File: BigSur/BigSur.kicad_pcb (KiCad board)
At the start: 2 copper layers, 123.5 x 131.5 mm, 148 parts, among them J1 XT30PW-M, J10 XT30PW-M, J12 XT30PW-M, J14 XT30PW-M, J15 XT30PW-M, J16 XT30PW-M, J2 XT30PW-M, J3 XT30PW-M, J4 XT30PW-M, J5 XT30PW-M, J6 XT30PW-M, J7 XT30PW-M, J8 XT30PW-M, J9 XT30PW-M, K1 G5LE-1A-VDDC12, K2 G5LE-1A-VDDC12, K3 G5LE-1A-VDDC12, K4 G5LE-1A-VDDC12, Q1 TSM900N10, Q2 TSM900N10, Q3 MMBT3904-7-F, Q4 MMBT3904-7-F, Q5 MMBT3904-7-F, Q6 MMBT3904-7-F, U1 DRV103H, U10 MCP6L02T-E_MS, U11 74LVC1G08W5-7, U12 ACS70331EESATR-2P5U3, U2 DRV103H, U3 DRV8806, U4 SMD46, U5 ACS70331EESATR-2P5U3, U6 ACS70331EESATR-2P5U3, U7 ACS70331EESATR-2P5U3, U8 ACS70331EESATR-2P5U3, U9 ACS70331EESATR-2P5U3

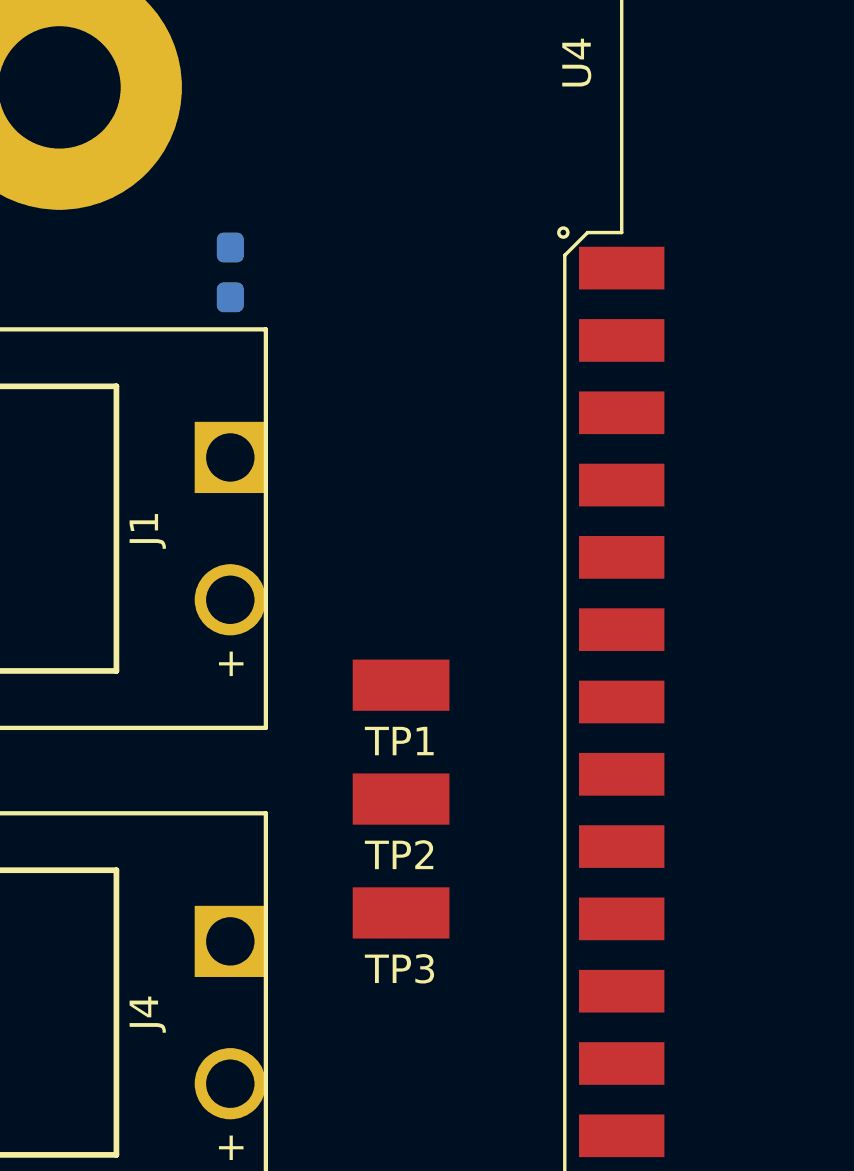
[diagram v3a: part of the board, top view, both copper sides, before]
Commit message: Added power LEDs.
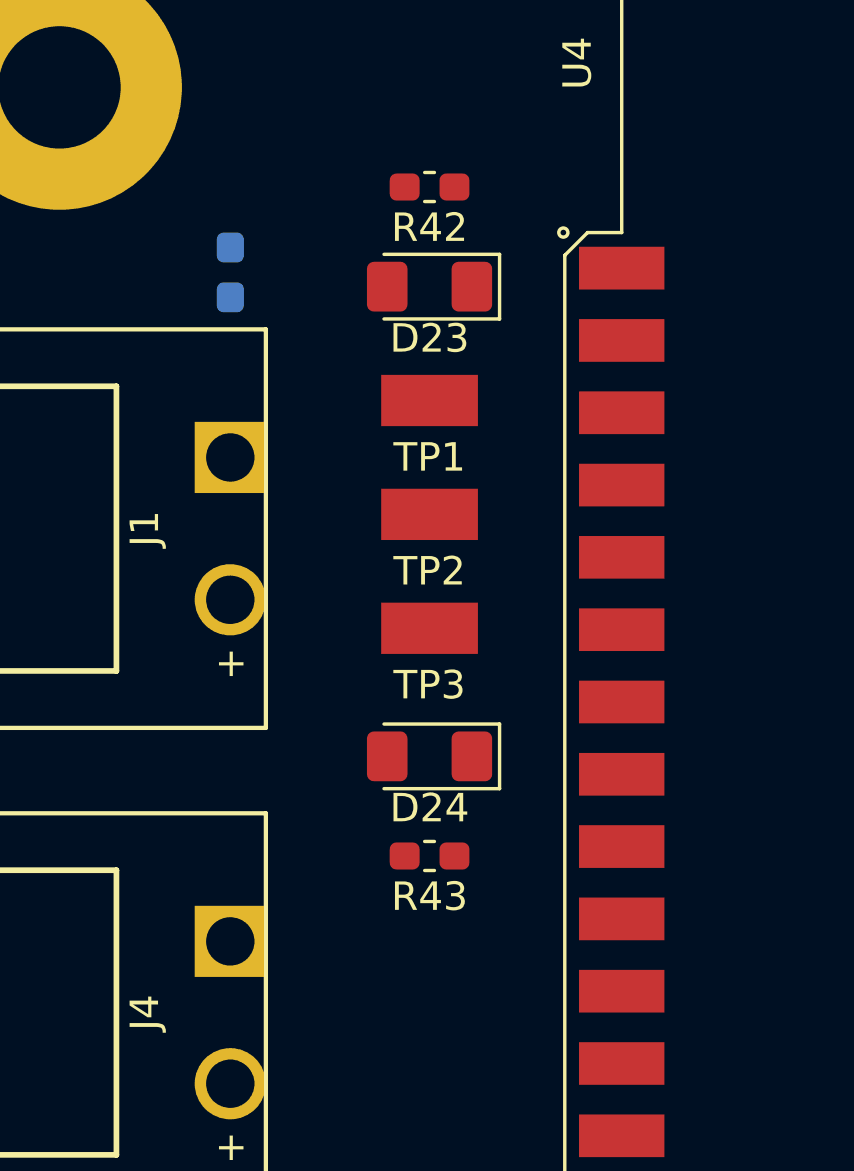
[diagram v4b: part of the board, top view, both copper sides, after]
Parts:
- added D23: QTLP651C4TR, LED_SMD:LED_1206_3216Metric_Pad1.42x1.75mm_HandSolder, F.Cu at (46.0, 34.5)
- added D24: QTLP651C4TR, LED_SMD:LED_1206_3216Metric_Pad1.42x1.75mm_HandSolder, F.Cu at (46.0, 51.0)
- added R42: 2K, Resistor_SMD:R_0603_1608Metric_Pad1.05x0.95mm_HandSolder, F.Cu at (46.0, 31.0)
- added R43: 1K, Resistor_SMD:R_0603_1608Metric_Pad1.05x0.95mm_HandSolder, F.Cu at (46.0, 54.5)
- moved TP1 10.0 mm to (46.0, 38.5)
- moved TP2 10.0 mm to (46.0, 42.5)
- moved TP3 10.0 mm to (46.0, 46.5)
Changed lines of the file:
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@@
     (tracks 0)
     (zones 0)
-    (modules 148)
-    (nets 116)
+    (modules 152)
+    (nets 118)
   )
   (page A4)
@@
   (net 114 "Net-(U10-Pad7)")
   (net 115 "Net-(U12-Pad7)")
+  (net 116 "Net-(D23-Pad1)")
+  (net 117 "Net-(D24-Pad1)")
   (net_class Default "This is the default net class."
     (clearance 0.2)
@@
     (add_net "Net-(D21-Pad2)")
     (add_net "Net-(D22-Pad2)")
+    (add_net "Net-(D23-Pad1)")
+    (add_net "Net-(D24-Pad1)")
     (add_net "Net-(D4-Pad2)")
     (add_net "Net-(D6-Pad2)")
@@
   )
   (module BigSur:Keystone_TP_SMD_5015 (layer F.Cu)
-    (at 45 48.5)
+    (at 46 38.5)
     (fp_text reference TP1 (at 0 2) (layer F.SilkS)
       (effects (font (size 1 1) (thickness 0.15)))
@@
   )
   (module BigSur:Keystone_TP_SMD_5015 (layer F.Cu)
-    (at 45 52.5)
+    (at 46 42.5)
     (fp_text reference TP2 (at 0 2) (layer F.SilkS)
       (effects (font (size 1 1) (thickness 0.15)))
@@
   )
   (module BigSur:Keystone_TP_SMD_5015 (layer F.Cu)
-    (at 45 56.5)
+    (at 46 46.5)
     (fp_text reference TP3 (at 0 2) (layer F.SilkS)
       (effects (font (size 1 1) (thickness 0.15)))
@@
       (net 7 +3V3))
   )
+  (module LED_SMD:LED_1206_3216Metric_Pad1.42x1.75mm_HandSolder (layer F.Cu)
+    (at 46 34.5 180)
+    (descr "LED SMD 1206 (3216 Metric), square (rectangular) end terminal, IPC_7351 nominal, (Body size source: http://www.tortai-tech.com/upload/download/2011102023233369053.pdf), generated with kicad-footprint-generator")
+    (tags "LED handsolder")
+    (attr smd)
+    (fp_text reference D23 (at 0 -1.82) (layer F.SilkS)
+      (effects (font (size 1 1) (thickness 0.15)))
+    )
+    (fp_text value QTLP651C4TR (at 0 1.82) (layer F.Fab)
+      (effects (font (size 1 1) (thickness 0.15)))
+    )
+    (fp_text user %R (at 0 0) (layer F.Fab)
+      (effects (font (size 0.8 0.8) (thickness 0.12)))
+    )
+    (fp_line (start 2.45 1.12) (end -2.45 1.12) (layer F.CrtYd) (width 0.05))
+    (fp_line (start 2.45 -1.12) (end 2.45 1.12) (layer F.CrtYd) (width 0.05))
+    (fp_line (start -2.45 -1.12) (end 2.45 -1.12) (layer F.CrtYd) (width 0.05))
+    (fp_line (start -2.45 1.12) (end -2.45 -1.12) (layer F.CrtYd) (width 0.05))
+    (fp_line (start -2.46 1.135) (end 1.6 1.135) (layer F.SilkS) (width 0.12))
+    (fp_line (start -2.46 -1.135) (end -2.46 1.135) (layer F.SilkS) (width 0.12))
+    (fp_line (start 1.6 -1.135) (end -2.46 -1.135) (layer F.SilkS) (width 0.12))
+    (fp_line (start 1.6 0.8) (end 1.6 -0.8) (layer F.Fab) (width 0.1))
+    (fp_line (start -1.6 0.8) (end 1.6 0.8) (layer F.Fab) (width 0.1))
+    (fp_line (start -1.6 -0.4) (end -1.6 0.8) (layer F.Fab) (width 0.1))
+    (fp_line (start -1.2 -0.8) (end -1.6 -0.4) (layer F.Fab) (width 0.1))
+    (fp_line (start 1.6 -0.8) (end -1.2 -0.8) (layer F.Fab) (width 0.1))
+    (pad 2 smd roundrect (at 1.4875 0 180) (size 1.425 1.75) (layers F.Cu F.Paste F.Mask) (roundrect_rratio 0.175439)
+      (net 2 +24V))
+    (pad 1 smd roundrect (at -1.4875 0 180) (size 1.425 1.75) (layers F.Cu F.Paste F.Mask) (roundrect_rratio 0.175439)
+      (net 116 "Net-(D23-Pad1)"))
+    (model ${KISYS3DMOD}/LED_SMD.3dshapes/LED_1206_3216Metric.wrl
+      (at (xyz 0 0 0))
+      (scale (xyz 1 1 1))
+      (rotate (xyz 0 0 0))
+    )
+  )
+  (module LED_SMD:LED_1206_3216Metric_Pad1.42x1.75mm_HandSolder (layer F.Cu)
+    (at 46 51 180)
+    (descr "LED SMD 1206 (3216 Metric), square (rectangular) end terminal, IPC_7351 nominal, (Body size source: http://www.tortai-tech.com/upload/download/2011102023233369053.pdf), generated with kicad-footprint-generator")
+    (tags "LED handsolder")
+    (attr smd)
+    (fp_text reference D24 (at 0 -1.82) (layer F.SilkS)
+      (effects (font (size 1 1) (thickness 0.15)))
+    )
+    (fp_text value QTLP651C4TR (at 0 1.82) (layer F.Fab)
+      (effects (font (size 1 1) (thickness 0.15)))
+    )
+    (fp_line (start 1.6 -0.8) (end -1.2 -0.8) (layer F.Fab) (width 0.1))
+    (fp_line (start -1.2 -0.8) (end -1.6 -0.4) (layer F.Fab) (width 0.1))
+    (fp_line (start -1.6 -0.4) (end -1.6 0.8) (layer F.Fab) (width 0.1))
+    (fp_line (start -1.6 0.8) (end 1.6 0.8) (layer F.Fab) (width 0.1))
+    (fp_line (start 1.6 0.8) (end 1.6 -0.8) (layer F.Fab) (width 0.1))
+    (fp_line (start 1.6 -1.135) (end -2.46 -1.135) (layer F.SilkS) (width 0.12))
+    (fp_line (start -2.46 -1.135) (end -2.46 1.135) (layer F.SilkS) (width 0.12))
+    (fp_line (start -2.46 1.135) (end 1.6 1.135) (layer F.SilkS) (width 0.12))
+    (fp_line (start -2.45 1.12) (end -2.45 -1.12) (layer F.CrtYd) (width 0.05))
+    (fp_line (start -2.45 -1.12) (end 2.45 -1.12) (layer F.CrtYd) (width 0.05))
+    (fp_line (start 2.45 -1.12) (end 2.45 1.12) (layer F.CrtYd) (width 0.05))
+    (fp_line (start 2.45 1.12) (end -2.45 1.12) (layer F.CrtYd) (width 0.05))
+    (fp_text user %R (at 0 0) (layer F.Fab)
+      (effects (font (size 0.8 0.8) (thickness 0.12)))
+    )
+    (pad 1 smd roundrect (at -1.4875 0 180) (size 1.425 1.75) (layers F.Cu F.Paste F.Mask) (roundrect_rratio 0.175439)
+      (net 117 "Net-(D24-Pad1)"))
+    (pad 2 smd roundrect (at 1.4875 0 180) (size 1.425 1.75) (layers F.Cu F.Paste F.Mask) (roundrect_rratio 0.175439)
+      (net 36 +12V))
+    (model ${KISYS3DMOD}/LED_SMD.3dshapes/LED_1206_3216Metric.wrl
+      (at (xyz 0 0 0))
+      (scale (xyz 1 1 1))
+      (rotate (xyz 0 0 0))
+    )
+  )
+  (module Resistor_SMD:R_0603_1608Metric_Pad1.05x0.95mm_HandSolder (layer F.Cu)
+    (at 46 31 180)
+    (descr "Resistor SMD 0603 (1608 Metric), square (rectangular) end terminal, IPC_7351 nominal with elongated pad for handsoldering. (Body size source: http://www.tortai-tech.com/upload/download/2011102023233369053.pdf), generated with kicad-footprint-generator")
+    (tags "resistor handsolder")
+    (attr smd)
+    (fp_text reference R42 (at 0 -1.43) (layer F.SilkS)
+      (effects (font (size 1 1) (thickness 0.15)))
+    )
+    (fp_text value 2K (at 0 1.43) (layer F.Fab)
+      (effects (font (size 1 1) (thickness 0.15)))
+    )
+    (fp_line (start -0.8 0.4) (end -0.8 -0.4) (layer F.Fab) (width 0.1))
+    (fp_line (start -0.8 -0.4) (end 0.8 -0.4) (layer F.Fab) (width 0.1))
+    (fp_line (start 0.8 -0.4) (end 0.8 0.4) (layer F.Fab) (width 0.1))
+    (fp_line (start 0.8 0.4) (end -0.8 0.4) (layer F.Fab) (width 0.1))
+    (fp_line (start -0.171267 -0.51) (end 0.171267 -0.51) (layer F.SilkS) (width 0.12))
+    (fp_line (start -0.171267 0.51) (end 0.171267 0.51) (layer F.SilkS) (width 0.12))
+    (fp_line (start -1.65 0.73) (end -1.65 -0.73) (layer F.CrtYd) (width 0.05))
+    (fp_line (start -1.65 -0.73) (end 1.65 -0.73) (layer F.CrtYd) (width 0.05))
+    (fp_line (start 1.65 -0.73) (end 1.65 0.73) (layer F.CrtYd) (width 0.05))
+    (fp_line (start 1.65 0.73) (end -1.65 0.73) (layer F.CrtYd) (width 0.05))
+    (fp_text user %R (at 0 0) (layer F.Fab)
+      (effects (font (size 0.4 0.4) (thickness 0.06)))
+    )
+    (pad 1 smd roundrect (at -0.875 0 180) (size 1.05 0.95) (layers F.Cu F.Paste F.Mask) (roundrect_rratio 0.25)
+      (net 116 "Net-(D23-Pad1)"))
+    (pad 2 smd roundrect (at 0.875 0 180) (size 1.05 0.95) (layers F.Cu F.Paste F.Mask) (roundrect_rratio 0.25)
+      (net 1 GND))
+    (model ${KISYS3DMOD}/Resistor_SMD.3dshapes/R_0603_1608Metric.wrl
+      (at (xyz 0 0 0))
+      (scale (xyz 1 1 1))
+      (rotate (xyz 0 0 0))
+    )
+  )
+  (module Resistor_SMD:R_0603_1608Metric_Pad1.05x0.95mm_HandSolder (layer F.Cu)
+    (at 46 54.5 180)
+    (descr "Resistor SMD 0603 (1608 Metric), square (rectangular) end terminal, IPC_7351 nominal with elongated pad for handsoldering. (Body size source: http://www.tortai-tech.com/upload/download/2011102023233369053.pdf), generated with kicad-footprint-generator")
+    (tags "resistor handsolder")
+    (attr smd)
+    (fp_text reference R43 (at 0 -1.43) (layer F.SilkS)
+      (effects (font (size 1 1) (thickness 0.15)))
+    )
+    (fp_text value 1K (at 0 1.43) (layer F.Fab)
+      (effects (font (size 1 1) (thickness 0.15)))
+    )
+    (fp_text user %R (at 0 0) (layer F.Fab)
+      (effects (font (size 0.4 0.4) (thickness 0.06)))
+    )
+    (fp_line (start 1.65 0.73) (end -1.65 0.73) (layer F.CrtYd) (width 0.05))
+    (fp_line (start 1.65 -0.73) (end 1.65 0.73) (layer F.CrtYd) (width 0.05))
+    (fp_line (start -1.65 -0.73) (end 1.65 -0.73) (layer F.CrtYd) (width 0.05))
+    (fp_line (start -1.65 0.73) (end -1.65 -0.73) (layer F.CrtYd) (width 0.05))
+    (fp_line (start -0.171267 0.51) (end 0.171267 0.51) (layer F.SilkS) (width 0.12))
+    (fp_line (start -0.171267 -0.51) (end 0.171267 -0.51) (layer F.SilkS) (width 0.12))
+    (fp_line (start 0.8 0.4) (end -0.8 0.4) (layer F.Fab) (width 0.1))
+    (fp_line (start 0.8 -0.4) (end 0.8 0.4) (layer F.Fab) (width 0.1))
+    (fp_line (start -0.8 -0.4) (end 0.8 -0.4) (layer F.Fab) (width 0.1))
+    (fp_line (start -0.8 0.4) (end -0.8 -0.4) (layer F.Fab) (width 0.1))
+    (pad 2 smd roundrect (at 0.875 0 180) (size 1.05 0.95) (layers F.Cu F.Paste F.Mask) (roundrect_rratio 0.25)
+      (net 1 GND))
+    (pad 1 smd roundrect (at -0.875 0 180) (size 1.05 0.95) (layers F.Cu F.Paste F.Mask) (roundrect_rratio 0.25)
+      (net 117 "Net-(D24-Pad1)"))
+    (model ${KISYS3DMOD}/Resistor_SMD.3dshapes/R_0603_1608Metric.wrl
+      (at (xyz 0 0 0))
+      (scale (xyz 1 1 1))
+      (rotate (xyz 0 0 0))
+    )
+  )
   (gr_arc (start 142.5 145) (end 142.5 152) (angle -90) (layer Edge.Cuts) (width 0.05))
